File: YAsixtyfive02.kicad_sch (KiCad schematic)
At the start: 61 parts, among them J1 ~{NMI}, J2 Aux 5VDC, J3 Power 5V, J4 Expansion Bus, J7 GND, J8 FTDI Serial2USB, SW1 RESET, SW2 SW_Push_DPDT, U1 WD65C02, U10 74LS138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

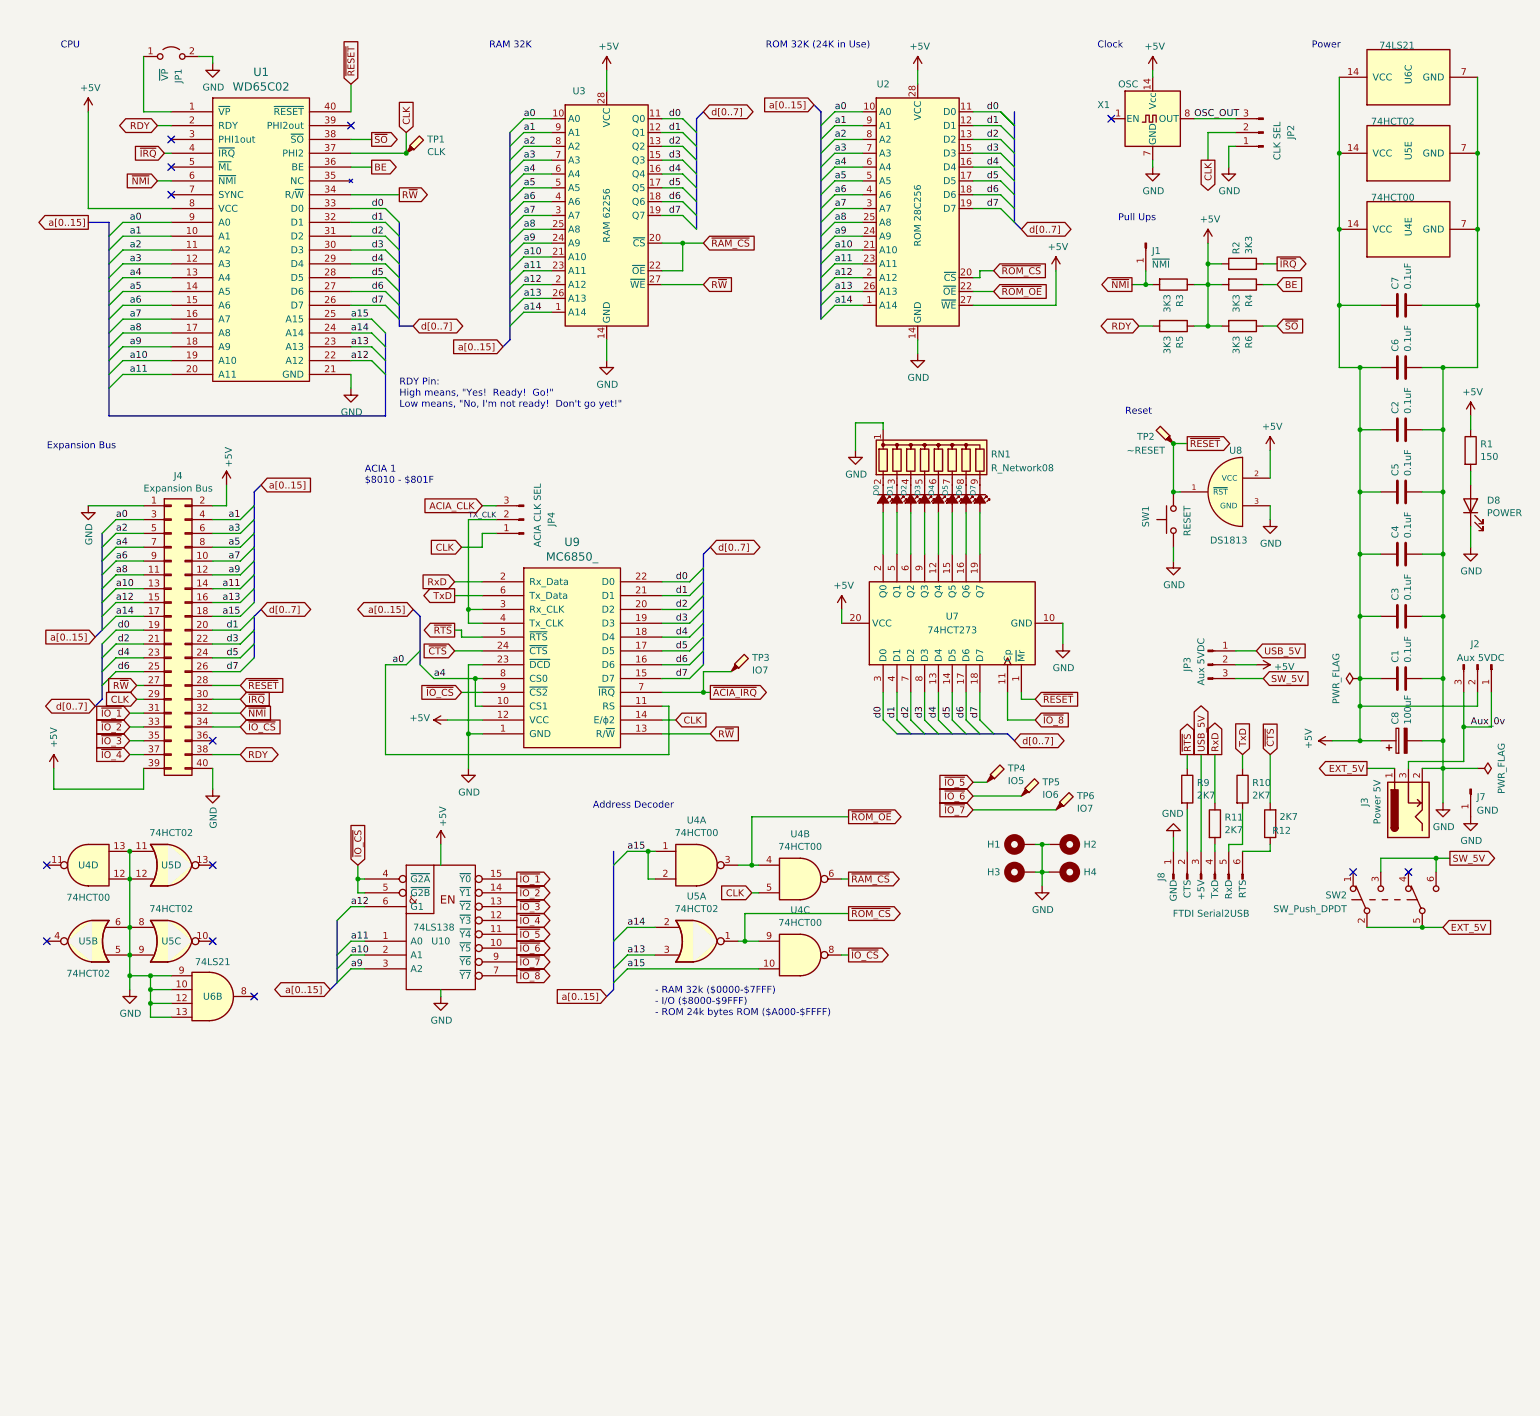
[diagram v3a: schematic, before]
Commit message: Deleted unused gate, ERC passed
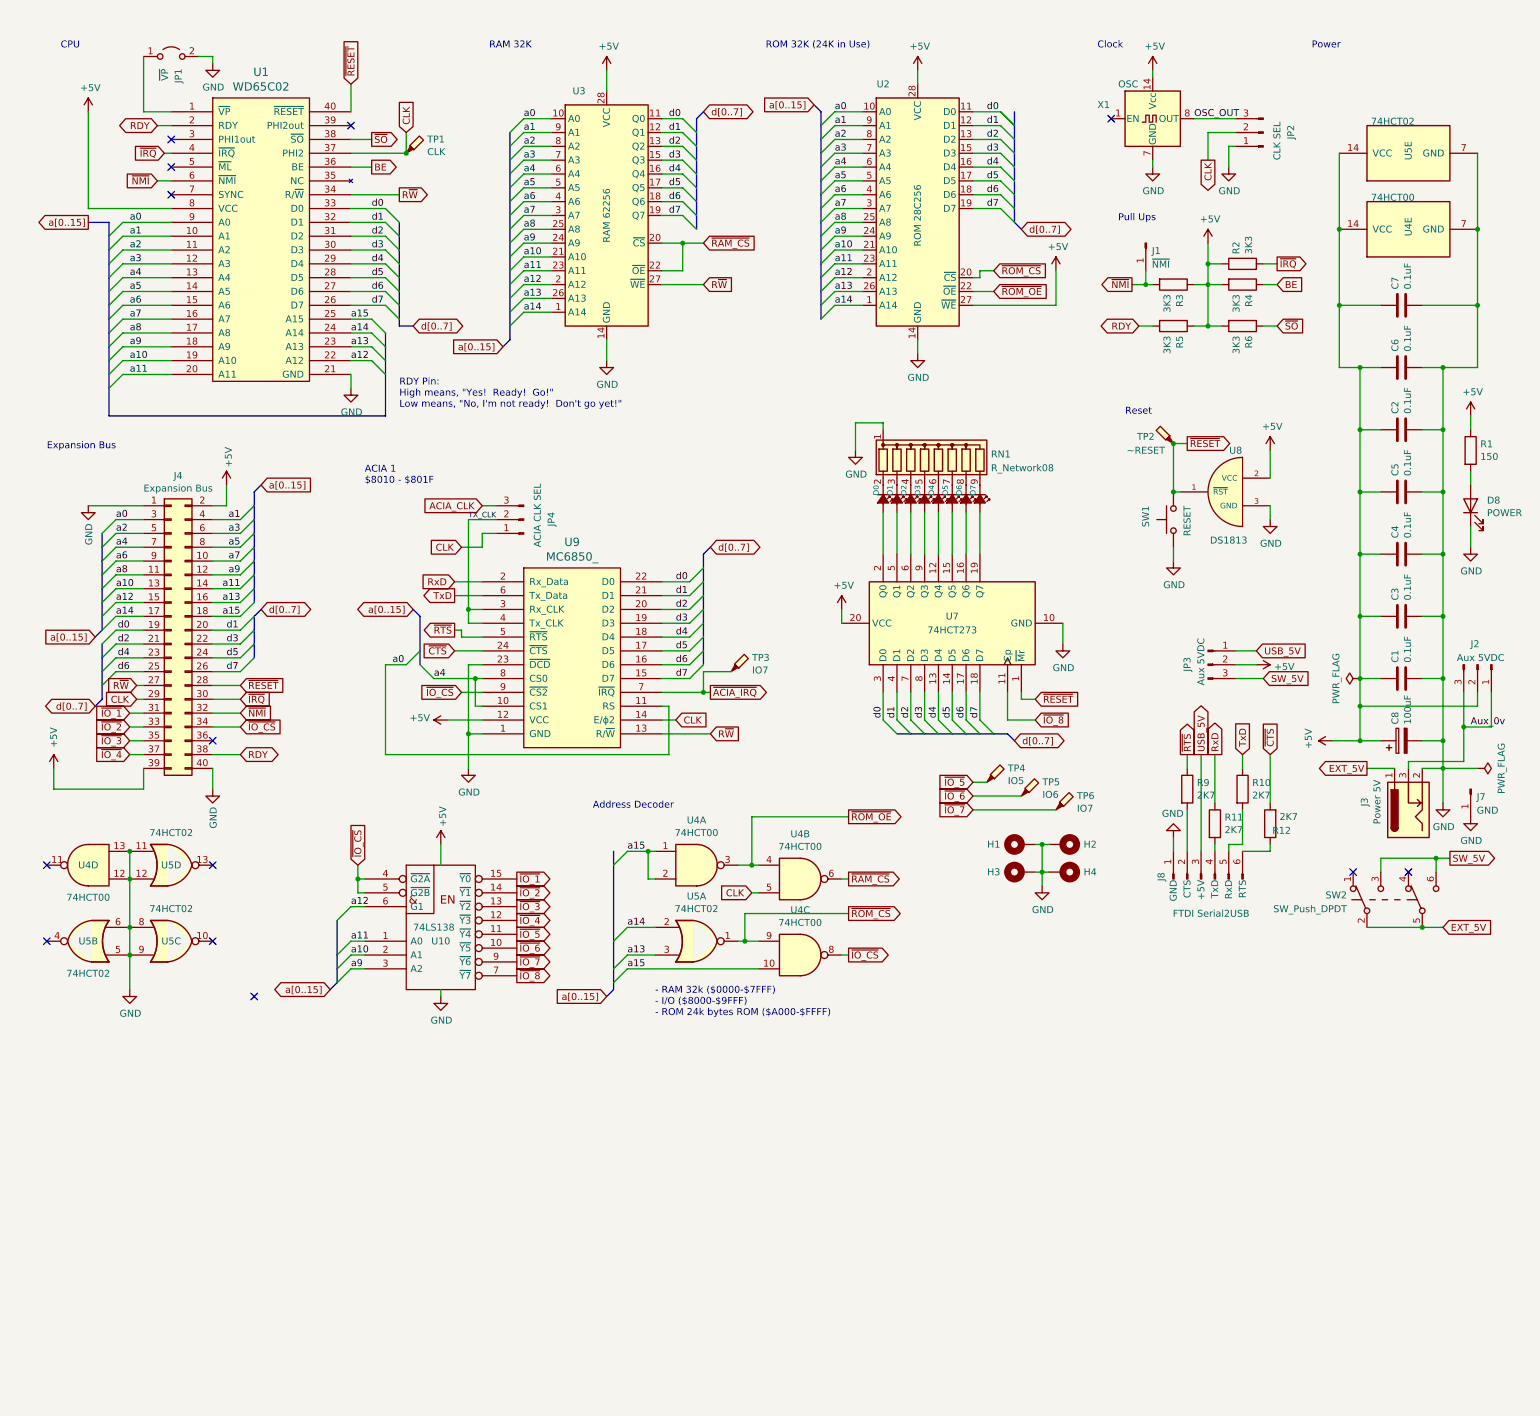
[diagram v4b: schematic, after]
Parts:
- removed U6: 74LS21, Package_DIP:DIP-14_W7.62mm_Socket_LongPads, symbol 74xx:74LS21
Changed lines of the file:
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@@
   (junction (at 273.05 143.51) (diameter 0) (color 0 0 0 0)
   )
-  (junction (at 35.56 189.23) (diameter 0) (color 0 0 0 0)
-  )
   (junction (at 73.66 168.91) (diameter 0) (color 0 0 0 0)
   )
@@
   (junction (at 276.86 140.97) (diameter 0) (color 0 0 0 0)
   )
-  (junction (at 279.4 35.56) (diameter 0) (color 0 0 0 0)
-  )
   (junction (at 257.81 120.65) (diameter 0) (color 0 0 0 0)
   )
@@
   (junction (at 137.16 134.62) (diameter 0) (color 0 0 0 0)
   )
-  (junction (at 31.75 186.69) (diameter 0) (color 0 0 0 0)
-  )
   (junction (at 273.05 132.08) (diameter 0) (color 0 0 0 0)
   )
-  (junction (at 35.56 186.69) (diameter 0) (color 0 0 0 0)
-  )
   (junction (at 269.24 177.8) (diameter 0) (color 0 0 0 0)
   )
@@
   (junction (at 273.05 74.93) (diameter 0) (color 0 0 0 0)
   )
-  (junction (at 35.56 191.77) (diameter 0) (color 0 0 0 0)
-  )
   (junction (at 199.39 162.56) (diameter 0) (color 0 0 0 0)
   )
@@
   (junction (at 93.98 119.38) (diameter 0) (color 0 0 0 0)
   )
-  (junction (at 254 35.56) (diameter 0) (color 0 0 0 0)
-  )
   (junction (at 144.78 180.34) (diameter 0) (color 0 0 0 0)
   )
@@
     (stroke (width 0) (type default) (color 0 0 0 0))
   )
-  (wire (pts (xy 31.75 186.69) (xy 31.75 189.23))
-    (stroke (width 0) (type default) (color 0 0 0 0))
-  )
   (bus (pts (xy 190.5 142.24) (xy 187.96 142.24))
     (stroke (width 0) (type default) (color 0 0 0 0))
@@
     (stroke (width 0) (type default) (color 0 0 0 0))
   )
-  (wire (pts (xy 254 35.56) (xy 254 21.59))
-    (stroke (width 0) (type default) (color 0 0 0 0))
-  )
   (bus (pts (xy 194.31 35.56) (xy 194.31 38.1))
     (stroke (width 0) (type default) (color 0 0 0 0))
@@
     (stroke (width 0) (type default) (color 0 0 0 0))
   )
-  (wire (pts (xy 35.56 194.31) (xy 35.56 191.77))
-    (stroke (width 0) (type default) (color 0 0 0 0))
-  )
   (wire (pts (xy 257.81 86.36) (xy 257.81 74.93))
     (stroke (width 0) (type default) (color 0 0 0 0))
@@
     (stroke (width 0) (type default) (color 0 0 0 0))
   )
-  (wire (pts (xy 39.37 189.23) (xy 35.56 189.23))
-    (stroke (width 0) (type default) (color 0 0 0 0))
-  )
   (wire (pts (xy 223.52 88.9) (xy 223.52 97.79))
     (stroke (width 0) (type default) (color 0 0 0 0))
@@
     (stroke (width 0) (type default) (color 0 0 0 0))
   )
-  (wire (pts (xy 39.37 194.31) (xy 35.56 194.31))
-    (stroke (width 0) (type default) (color 0 0 0 0))
-  )
   (bus (pts (xy 182.88 142.24) (xy 180.34 142.24))
     (stroke (width 0) (type default) (color 0 0 0 0))
@@
     (stroke (width 0) (type default) (color 0 0 0 0))
   )
-  (wire (pts (xy 31.75 182.88) (xy 31.75 186.69))
+  (wire (pts (xy 31.75 182.88) (xy 31.75 189.23))
     (stroke (width 0) (type default) (color 0 0 0 0))
   )
@@
     (stroke (width 0) (type default) (color 0 0 0 0))
   )
-  (wire (pts (xy 35.56 186.69) (xy 31.75 186.69))
-    (stroke (width 0) (type default) (color 0 0 0 0))
-  )
   (wire (pts (xy 161.29 27.94) (xy 166.37 27.94))
     (stroke (width 0) (type default) (color 0 0 0 0))
@@
     (stroke (width 0) (type default) (color 0 0 0 0))
   )
-  (wire (pts (xy 279.4 35.56) (xy 279.4 21.59))
-    (stroke (width 0) (type default) (color 0 0 0 0))
-  )
   (wire (pts (xy 273.05 132.08) (xy 273.05 143.51))
     (stroke (width 0) (type default) (color 0 0 0 0))
@@
     (stroke (width 0) (type default) (color 0 0 0 0))
   )
-  (wire (pts (xy 35.56 189.23) (xy 35.56 186.69))
-    (stroke (width 0) (type default) (color 0 0 0 0))
-  )
   (wire (pts (xy 232.41 55.88) (xy 229.87 55.88))
     (stroke (width 0) (type default) (color 0 0 0 0))
@@
     (stroke (width 0) (type default) (color 0 0 0 0))
   )
-  (wire (pts (xy 35.56 191.77) (xy 35.56 189.23))
-    (stroke (width 0) (type default) (color 0 0 0 0))
-  )
   (bus (pts (xy 135.89 41.91) (xy 135.89 44.45))
     (stroke (width 0) (type default) (color 0 0 0 0))
@@
     (stroke (width 0) (type default) (color 0 0 0 0))
   )
-  (wire (pts (xy 39.37 186.69) (xy 35.56 186.69))
-    (stroke (width 0) (type default) (color 0 0 0 0))
-  )
   (wire (pts (xy 39.37 58.42) (xy 30.48 58.42))
     (stroke (width 0) (type default) (color 0 0 0 0))
@@
     (stroke (width 0) (type default) (color 0 0 0 0))
   )
-  (wire (pts (xy 39.37 191.77) (xy 35.56 191.77))
-    (stroke (width 0) (type default) (color 0 0 0 0))
-  )
   (wire (pts (xy 223.52 163.83) (xy 223.52 161.29))
     (stroke (width 0) (type default) (color 0 0 0 0))
@@
     (pin "1")
   )
-  (symbol (lib_id "74xx:74LS21") (at 46.99 190.5 0) (unit 2)
-    (in_bom yes) (on_board yes)
-    (property "Reference" "U6" (id 0) (at 46.99 190.5 0))
-    (property "Value" "74LS21" (id 1) (at 46.99 184.15 0))
-    (property "Footprint" "Package_DIP:DIP-14_W7.62mm_Socket_LongPads" (id 2) (at 46.99 190.5 0)
-      (effects (font (size 1.27 1.27)) hide)
-    )
-    (property "Datasheet" "http://www.ti.com/lit/gpn/sn74LS21" (id 3) (at 46.99 190.5 0)
-      (effects (font (size 1.27 1.27)) hide)
-    )
-    (pin "1")
-    (pin "2")
-    (pin "4")
-    (pin "5")
-    (pin "6")
-    (pin "10")
-    (pin "12")
-    (pin "13")
-    (pin "8")
-    (pin "9")
-    (pin "14")
-    (pin "7")
-  )
-  (symbol (lib_id "74xx:74LS21") (at 266.7 21.59 90) (unit 3)
-    (in_bom yes) (on_board yes)
-    (property "Reference" "U6" (id 0) (at 266.7 22.86 0)
-      (effects (font (size 1.27 1.27)) (justify left))
-    )
-    (property "Value" "74LS21" (id 1) (at 267.843 15.748 90)
-      (effects (font (size 1.27 1.27)) (justify left))
-    )
-    (property "Footprint" "Package_DIP:DIP-14_W7.62mm_Socket_LongPads" (id 2) (at 266.7 21.59 0)
-      (effects (font (size 1.27 1.27)) hide)
-    )
-    (property "Datasheet" "http://www.ti.com/lit/gpn/sn74LS21" (id 3) (at 266.7 21.59 0)
-      (effects (font (size 1.27 1.27)) hide)
-    )
-    (pin "1")
-    (pin "2")
-    (pin "4")
-    (pin "5")
-    (pin "6")
-    (pin "10")
-    (pin "12")
-    (pin "13")
-    (pin "8")
-    (pin "9")
-    (pin "14")
-    (pin "7")
-  )
   (symbol (lib_id "Connector_Generic:Conn_02x20_Odd_Even") (at 39.37 123.19 0) (unit 1)
     (in_bom yes) (on_board yes)
@@
       (reference "U5") (unit 5) (value "74HCT02") (footprint "Package_DIP:DIP-14_W7.62mm_Socket_LongPads")
     )
-    (path "/00000000-0000-0000-0000-000061b48f07"
-      (reference "U6") (unit 2) (value "74LS21") (footprint "Package_DIP:DIP-14_W7.62mm_Socket_LongPads")
-    )
-    (path "/00000000-0000-0000-0000-000061b4de7c"
-      (reference "U6") (unit 3) (value "74LS21") (footprint "Package_DIP:DIP-14_W7.62mm_Socket_LongPads")
-    )
     (path "/68bf858e-c314-4ec4-bfab-c7ff755c91c4"

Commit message: Test Pads Footprint Changed
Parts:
- TP4, TP5, TP6: footprint TestPoint:TestPoint_THTPad_2.0x2.0mm_Drill1.0mm -> TestPoint:TestPoint_THTPad_1.0x1.0mm_Drill0.5mm
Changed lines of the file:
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@@
       (effects (font (size 1.27 1.27)) (justify left))
     )
-    (property "Footprint" "TestPoint:TestPoint_THTPad_2.0x2.0mm_Drill1.0mm" (id 2) (at 207.01 156.21 0)
+    (property "Footprint" "TestPoint:TestPoint_THTPad_1.0x1.0mm_Drill0.5mm" (id 2) (at 207.01 156.21 0)
       (effects (font (size 1.27 1.27)) hide)
     )
@@
       (effects (font (size 1.27 1.27)) (justify left))
     )
-    (property "Footprint" "TestPoint:TestPoint_THTPad_2.0x2.0mm_Drill1.0mm" (id 2) (at 194.31 151.13 0)
+    (property "Footprint" "TestPoint:TestPoint_THTPad_1.0x1.0mm_Drill0.5mm" (id 2) (at 194.31 151.13 0)
       (effects (font (size 1.27 1.27)) hide)
     )
@@
       (effects (font (size 1.27 1.27)) (justify left))
     )
-    (property "Footprint" "TestPoint:TestPoint_THTPad_2.0x2.0mm_Drill1.0mm" (id 2) (at 200.66 153.67 0)
+    (property "Footprint" "TestPoint:TestPoint_THTPad_1.0x1.0mm_Drill0.5mm" (id 2) (at 200.66 153.67 0)
       (effects (font (size 1.27 1.27)) hide)
     )
@@
     )
     (path "/50f6d03f-fd54-4133-b062-682e343debb8"
-      (reference "TP4") (unit 1) (value "IO5") (footprint "TestPoint:TestPoint_THTPad_2.0x2.0mm_Drill1.0mm")
+      (reference "TP4") (unit 1) (value "IO5") (footprint "TestPoint:TestPoint_THTPad_1.0x1.0mm_Drill0.5mm")
     )
     (path "/8276eb26-106b-49ba-8e02-d04faf35f0c9"
-      (reference "TP5") (unit 1) (value "IO6") (footprint "TestPoint:TestPoint_THTPad_2.0x2.0mm_Drill1.0mm")
+      (reference "TP5") (unit 1) (value "IO6") (footprint "TestPoint:TestPoint_THTPad_1.0x1.0mm_Drill0.5mm")
     )
     (path "/2733c48f-18fb-498f-8b30-fc79ccb809ef"
-      (reference "TP6") (unit 1) (value "IO7") (footprint "TestPoint:TestPoint_THTPad_2.0x2.0mm_Drill1.0mm")
+      (reference "TP6") (unit 1) (value "IO7") (footprint "TestPoint:TestPoint_THTPad_1.0x1.0mm_Drill0.5mm")
     )
     (path "/00000000-0000-0000-0000-0000612219a0"

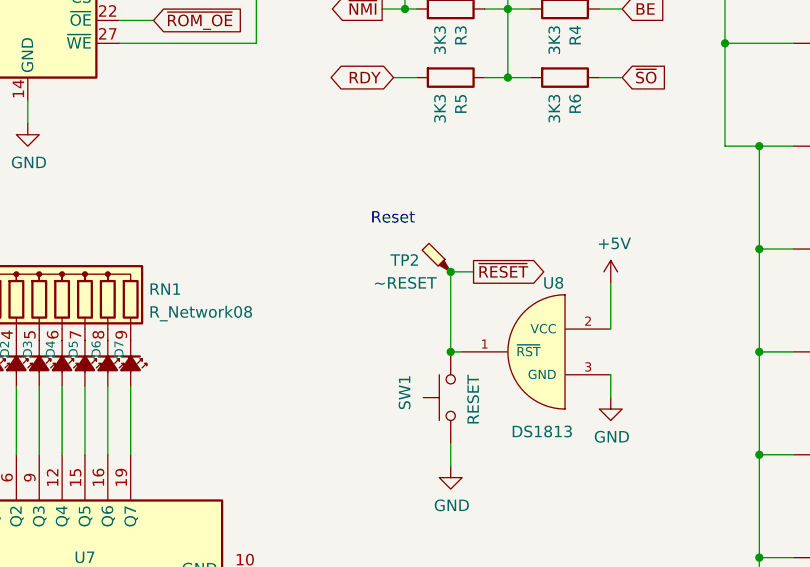
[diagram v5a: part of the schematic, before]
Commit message: COmponents placed ready to route
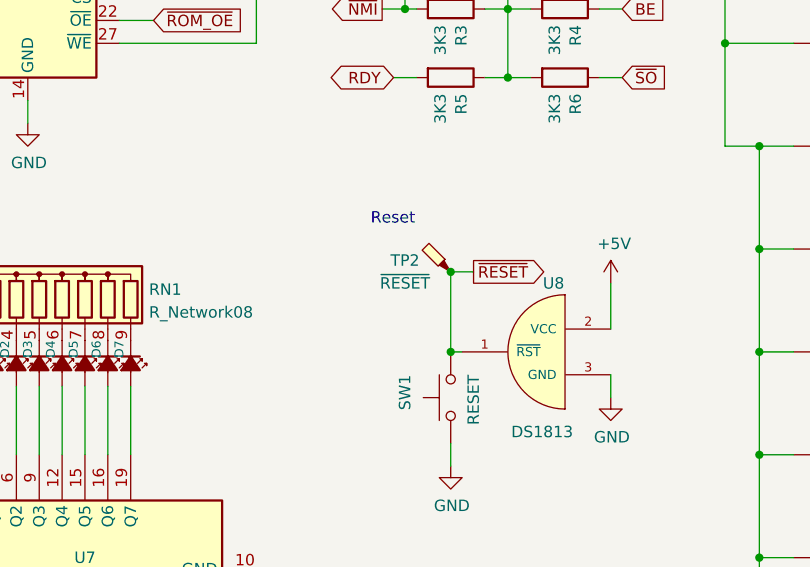
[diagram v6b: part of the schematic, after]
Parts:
- TP2: value ~RESET -> ~{RESET}
- TP3: footprint TestPoint:TestPoint_THTPad_2.0x2.0mm_Drill1.0mm -> TestPoint:TestPoint_THTPad_1.0x1.0mm_Drill0.5mm
- U10: footprint Package_DIP:DIP-16_W7.62mm_LongPads -> Package_DIP:DIP-16_W7.62mm_Socket_LongPads
- U9: footprint Package_DIP:DIP-24_W15.24mm_LongPads -> Package_DIP:DIP-24_W15.24mm_Socket_LongPads
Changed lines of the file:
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@@
       (effects (font (size 1.524 1.524)))
     )
-    (property "Footprint" "Package_DIP:DIP-24_W15.24mm_LongPads" (id 2) (at 113.03 144.78 0)
+    (property "Footprint" "Package_DIP:DIP-24_W15.24mm_Socket_LongPads" (id 2) (at 113.03 144.78 0)
       (effects (font (size 1.524 1.524)) hide)
     )
@@
     (in_bom yes) (on_board yes)
     (property "Reference" "TP2" (id 0) (at 218.44 87.63 90))
-    (property "Value" "~RESET" (id 1) (at 218.44 90.17 90))
+    (property "Value" "~{RESET}" (id 1) (at 218.44 90.17 90))
     (property "Footprint" "TestPoint:TestPoint_THTPad_2.0x2.0mm_Drill1.0mm" (id 2) (at 223.52 83.82 0)
       (effects (font (size 1.27 1.27)) hide)
@@
     (property "Reference" "U10" (id 0) (at 88.9 180.34 0))
     (property "Value" "74LS138" (id 1) (at 87.63 177.8 0))
-    (property "Footprint" "Package_DIP:DIP-16_W7.62mm_LongPads" (id 2) (at 88.9 173.99 0)
+    (property "Footprint" "Package_DIP:DIP-16_W7.62mm_Socket_LongPads" (id 2) (at 88.9 173.99 0)
       (effects (font (size 1.27 1.27)) hide)
     )
@@
       (effects (font (size 1.27 1.27)) (justify left))
     )
-    (property "Footprint" "TestPoint:TestPoint_THTPad_2.0x2.0mm_Drill1.0mm" (id 2) (at 147.32 130.81 0)
+    (property "Footprint" "TestPoint:TestPoint_THTPad_1.0x1.0mm_Drill0.5mm" (id 2) (at 147.32 130.81 0)
       (effects (font (size 1.27 1.27)) hide)
     )
@@
     )
     (path "/00000000-0000-0000-0000-000063d64eab"
-      (reference "TP2") (unit 1) (value "~RESET") (footprint "TestPoint:TestPoint_THTPad_2.0x2.0mm_Drill1.0mm")
+      (reference "TP2") (unit 1) (value "~{RESET}") (footprint "TestPoint:TestPoint_THTPad_2.0x2.0mm_Drill1.0mm")
     )
     (path "/75f85b84-9777-4d8b-a0f4-27c0e653b059"
-      (reference "TP3") (unit 1) (value "IO7") (footprint "TestPoint:TestPoint_THTPad_2.0x2.0mm_Drill1.0mm")
+      (reference "TP3") (unit 1) (value "IO7") (footprint "TestPoint:TestPoint_THTPad_1.0x1.0mm_Drill0.5mm")
     )
     (path "/50f6d03f-fd54-4133-b062-682e343debb8"
@@
     )
     (path "/00000000-0000-0000-0000-0000634754d5"
-      (reference "U9") (unit 1) (value "MC6850_") (footprint "Package_DIP:DIP-24_W15.24mm_LongPads")
+      (reference "U9") (unit 1) (value "MC6850_") (footprint "Package_DIP:DIP-24_W15.24mm_Socket_LongPads")
     )
     (path "/70cb47bf-9219-4417-98a4-88cbb4e37bcd"
-      (reference "U10") (unit 1) (value "74LS138") (footprint "Package_DIP:DIP-16_W7.62mm_LongPads")
+      (reference "U10") (unit 1) (value "74LS138") (footprint "Package_DIP:DIP-16_W7.62mm_Socket_LongPads")
     )
     (path "/00000000-0000-0000-0000-0000612a3428"
